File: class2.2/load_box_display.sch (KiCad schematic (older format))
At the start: 10 parts

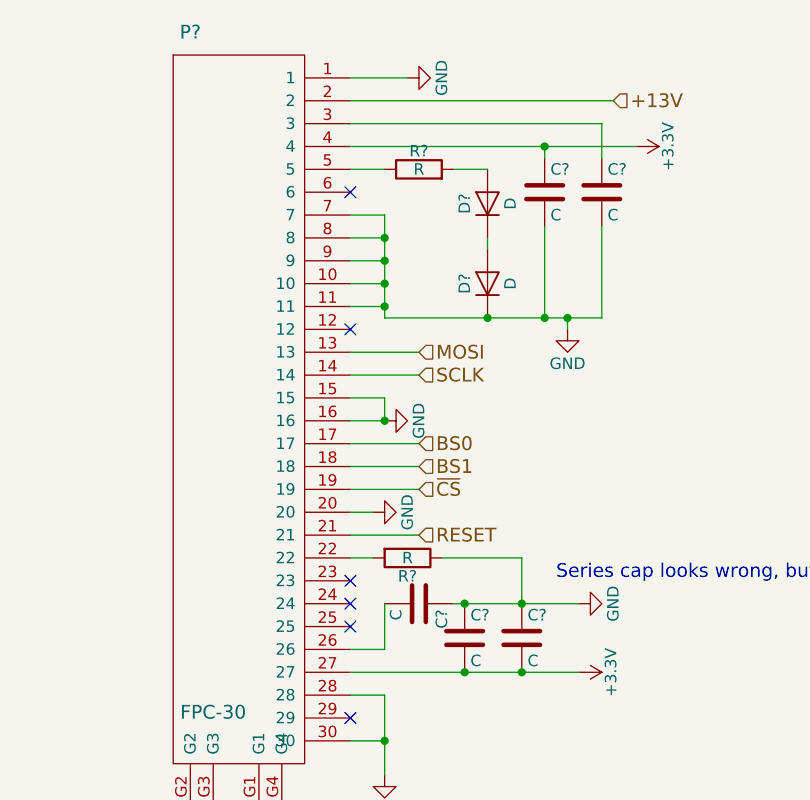
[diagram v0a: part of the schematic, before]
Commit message: Moving class2.2 forward, includes 13V switching converter.
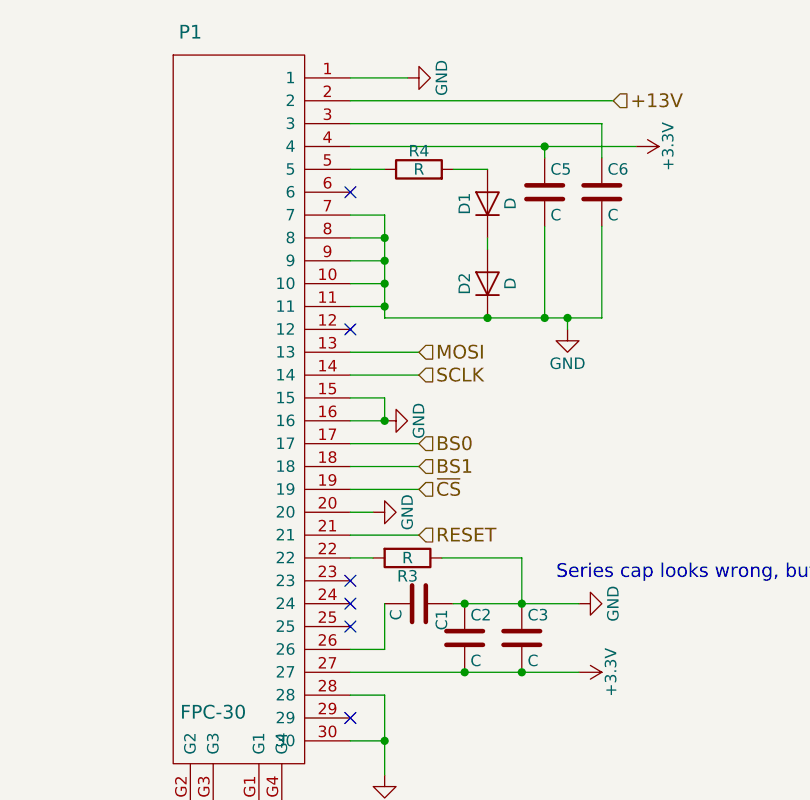
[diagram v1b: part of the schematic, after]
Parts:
- gave numbers to parts that had none: 10
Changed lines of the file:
@@
 LIBS:stm32
 LIBS:switches
+LIBS:ap3012
 LIBS:fpc
 LIBS:load_box-cache
@@
 $EndDescr
 $Comp
-L FPC-30 P?
+L FPC-30 P1
 U 1 1 58EFF997
 P 5200 3700
-F 0 "P?" H 5000 5600 60  0000 C CNN
+F 0 "P1" H 5000 5600 60  0000 C CNN
 F 1 "FPC-30" H 5100 2625 60  0000 C CNN
 F 2 "" H 5150 3700 60  0001 C CNN
@@
 $EndComp
 $Comp
-L GND #PWR?
+L GND #PWR10
 U 1 1 58EFFA17
 P 5950 2000
-F 0 "#PWR?" H 5950 1750 50  0001 C CNN
+F 0 "#PWR10" H 5950 1750 50  0001 C CNN
 F 1 "GND" H 5950 1850 50  0000 C CNN
 F 2 "" H 5950 2000 50  0001 C CNN
@@
 	6850 2100 5700 2100
 $Comp
-L GND #PWR?
+L GND #PWR11
 U 1 1 58EFFA94
 P 6650 3100
-F 0 "#PWR?" H 6650 2850 50  0001 C CNN
+F 0 "#PWR11" H 6650 2850 50  0001 C CNN
 F 1 "GND" H 6650 2950 50  0000 C CNN
 F 2 "" H 6650 3100 50  0001 C CNN
@@
 $EndComp
 $Comp
-L C C?
+L C C6
 U 1 1 58EFFAA3
 P 6800 2500
-F 0 "C?" H 6825 2600 50  0000 L CNN
+F 0 "C6" H 6825 2600 50  0000 L CNN
 F 1 "C" H 6825 2400 50  0000 L CNN
 F 2 "" H 6838 2350 50  0001 C CNN
@@
 $EndComp
 $Comp
-L C C?
+L C C5
 U 1 1 58EFFAC2
 P 6550 2500
-F 0 "C?" H 6575 2600 50  0000 L CNN
+F 0 "C5" H 6575 2600 50  0000 L CNN
 F 1 "C" H 6575 2400 50  0000 L CNN
 F 2 "" H 6588 2350 50  0001 C CNN
@@
 	6800 2200 6800 2350
 $Comp
-L +3.3V #PWR?
+L +3.3V #PWR14
 U 1 1 58EFFAF4
 P 6950 2300
-F 0 "#PWR?" H 6950 2150 50  0001 C CNN
+F 0 "#PWR14" H 6950 2150 50  0001 C CNN
 F 1 "+3.3V" H 6950 2440 50  0000 C CNN
 F 2 "" H 6950 2300 50  0001 C CNN
@@
 Connection ~ 6550 2300
 $Comp
-L D D?
+L D D1
 U 1 1 58EFFB58
 P 6300 2550
-F 0 "D?" H 6300 2650 50  0000 C CNN
+F 0 "D1" H 6300 2650 50  0000 C CNN
 F 1 "D" H 6300 2450 50  0000 C CNN
 F 2 "" H 6300 2550 50  0001 C CNN
@@
 $EndComp
 $Comp
-L D D?
+L D D2
 U 1 1 58EFFBF3
 P 6300 2900
-F 0 "D?" H 6300 3000 50  0000 C CNN
+F 0 "D2" H 6300 3000 50  0000 C CNN
 F 1 "D" H 6300 2800 50  0000 C CNN
 F 2 "" H 6300 2900 50  0001 C CNN
@@
 	6300 2750 6300 2700
 $Comp
-L R R?
+L R R4
 U 1 1 58EFFC7A
 P 6000 2400
-F 0 "R?" V 6080 2400 50  0000 C CNN
+F 0 "R4" V 6080 2400 50  0000 C CNN
 F 1 "R" V 6000 2400 50  0000 C CNN
 F 2 "" V 5930 2400 50  0001 C CNN
@@
 	6000 4000 5700 4000
 $Comp
-L R R?
+L R R3
 U 1 1 58F0008A
 P 5950 4100
-F 0 "R?" V 6030 4100 50  0000 C CNN
+F 0 "R3" V 6030 4100 50  0000 C CNN
 F 1 "R" V 5950 4100 50  0000 C CNN
 F 2 "" V 5880 4100 50  0001 C CNN
@@
 	5800 4100 5700 4100
 $Comp
-L C C?
+L C C2
 U 1 1 58F0013F
 P 6200 4450
-F 0 "C?" H 6225 4550 50  0000 L CNN
+F 0 "C2" H 6225 4550 50  0000 L CNN
 F 1 "C" H 6225 4350 50  0000 L CNN
 F 2 "" H 6238 4300 50  0001 C CNN
@@
 $EndComp
 $Comp
-L C C?
+L C C3
 U 1 1 58F001DC
 P 6450 4450
-F 0 "C?" H 6475 4550 50  0000 L CNN
+F 0 "C3" H 6475 4550 50  0000 L CNN
 F 1 "C" H 6475 4350 50  0000 L CNN
 F 2 "" H 6488 4300 50  0001 C CNN
@@
 Connection ~ 6200 4600
 $Comp
-L +3.3V #PWR?
+L +3.3V #PWR13
 U 1 1 58F0024F
 P 6700 4600
-F 0 "#PWR?" H 6700 4450 50  0001 C CNN
+F 0 "#PWR13" H 6700 4450 50  0001 C CNN
 F 1 "+3.3V" H 6700 4740 50  0000 C CNN
 F 2 "" H 6700 4600 50  0001 C CNN
@@
 	6450 4300 6450 4100
 $Comp
-L GND #PWR?
+L GND #PWR12
 U 1 1 58F0033A
 P 6700 4300
-F 0 "#PWR?" H 6700 4050 50  0001 C CNN
+F 0 "#PWR12" H 6700 4050 50  0001 C CNN
 F 1 "GND" H 6700 4150 50  0000 C CNN
 F 2 "" H 6700 4300 50  0001 C CNN
@@
 $EndComp
 $Comp
-L GND #PWR?
+L GND #PWR9
 U 1 1 58F003A8
 P 5850 5050
-F 0 "#PWR?" H 5850 4800 50  0001 C CNN
+F 0 "#PWR9" H 5850 4800 50  0001 C CNN
 F 1 "GND" H 5850 4900 50  0000 C CNN
 F 2 "" H 5850 5050 50  0001 C CNN
@@
 	6000 3600 5700 3600
 $Comp
-L GND #PWR?
+L GND #PWR8
 U 1 1 58F00650
 P 5850 3500
-F 0 "#PWR?" H 5850 3250 50  0001 C CNN
+F 0 "#PWR8" H 5850 3250 50  0001 C CNN
 F 1 "GND" H 5850 3350 50  0000 C CNN
 F 2 "" H 5850 3500 50  0001 C CNN
@@
 Connection ~ 5850 3500
 $Comp
-L GND #PWR?
+L GND #PWR7
 U 1 1 58F00678
 P 5800 3900
-F 0 "#PWR?" H 5800 3650 50  0001 C CNN
+F 0 "#PWR7" H 5800 3650 50  0001 C CNN
 F 1 "GND" H 5800 3750 50  0000 C CNN
 F 2 "" H 5800 3900 50  0001 C CNN
@@
 Series cap looks wrong, but pin 26 is regulated from VCI on pin 27
 $Comp
-L C C?
+L C C1
 U 1 1 58F009DF
 P 6000 4300
-F 0 "C?" H 6025 4400 50  0000 L CNN
+F 0 "C1" H 6025 4400 50  0000 L CNN
 F 1 "C" H 6025 4200 50  0000 L CNN
 F 2 "" H 6038 4150 50  0001 C CNN
